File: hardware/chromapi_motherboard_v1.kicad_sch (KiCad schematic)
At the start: 9 parts

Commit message: Updating BOM
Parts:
- H1: now left out of the parts list
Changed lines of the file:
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@@
 		(body_style 1)
 		(exclude_from_sim no)
-		(in_bom yes)
+		(in_bom no)
 		(on_board yes)
 		(in_pos_files yes)

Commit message: Adding MPN to parts
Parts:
- TP1: now left out of the parts list
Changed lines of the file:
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@@
+			)
+		)
+		(property "v" ""
+			(at 156.21 182.88 90)
+			(hide yes)
+			(show_name no)
+			(do_not_autoplace no)
+			(effects
+				(font
+					(size 1.27 1.27)
+				)
 			)
 		)
@@
 			)
 		)
+		(property "v" ""
+			(at 125.73 181.61 0)
+			(hide yes)
+			(show_name no)
+			(do_not_autoplace no)
+			(effects
+				(font
+					(size 1.27 1.27)
+				)
+			)
+		)
 		(instances
 			(project "chromapi_motherboard_v1"
@@
 			)
 		)
+		(property "v" ""
+			(at 149.86 182.88 90)
+			(hide yes)
+			(show_name no)
+			(do_not_autoplace no)
+			(effects
+				(font
+					(size 1.27 1.27)
+				)
+			)
+		)
 		(pin "1"
 		)
@@
 			)
 		)
+		(property "v" ""
+			(at 120.65 189.23 0)
+			(hide yes)
+			(show_name no)
+			(do_not_autoplace no)
+			(effects
+				(font
+					(size 1.27 1.27)
+				)
+			)
+		)
 		(instances
 			(project "chromapi_motherboard_v1"
@@
 			)
 		)
+		(property "v" ""
+			(at 115.57 181.61 0)
+			(hide yes)
+			(show_name no)
+			(do_not_autoplace no)
+			(effects
+				(font
+					(size 1.27 1.27)
+				)
+			)
+		)
 		(instances
 			(project "chromapi_motherboard_v1"
@@
 			)
 		)
+		(property "v" ""
+			(at 143.51 182.88 90)
+			(hide yes)
+			(show_name no)
+			(do_not_autoplace no)
+			(effects
+				(font
+					(size 1.27 1.27)
+				)
+			)
+		)
 		(pin "1"
 		)
@@
 			)
 		)
+		(property "v" ""
+			(at 134.62 168.91 0)
+			(hide yes)
+			(show_name no)
+			(do_not_autoplace no)
+			(effects
+				(font
+					(size 1.27 1.27)
+				)
+			)
+		)
 		(instances
 			(project "chromapi_motherboard_v1"
@@
 		(body_style 1)
 		(exclude_from_sim no)
-		(in_bom yes)
+		(in_bom no)
 		(on_board yes)
 		(in_pos_files yes)
@@
 		)
 		(property "MP" ""
+			(at 140.97 187.96 90)
+			(hide yes)
+			(show_name no)
+			(do_not_autoplace no)
+			(effects
+				(font
+					(size 1.27 1.27)
+				)
+			)
+		)
+		(property "v" ""
 			(at 140.97 187.96 90)
 			(hide yes)
@@
 			(at 162.56 182.88 90)
 			(hide yes)
+			(show_name no)
+			(do_not_autoplace no)
+			(effects
+				(font
+					(size 1.27 1.27)
+				)
+			)
+		)
+		(property "v" ""
+			(at 162.56 182.88 90)
+			(hide yes)

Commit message: Updating schematic
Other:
- note added: "15/04/2026"
- note removed: "JJ/03/2026"

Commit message: note on audio issue
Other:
- note added: "B1"
- note added: "XX/XX/2026"
- note added: "[fixed] correcting the polarity of the connectors for the servomotors"
- note added: "[todo] change the NRST label located on GPIO16 (RPI) to an available position"
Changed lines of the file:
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@@
 		(comment 1 "Ousmane THIONGANE")
+	)
+	(text "[todo] change the NRST label located on GPIO16 (RPI) to an available position"
+		(exclude_from_sim no)
+		(at 182.118 44.704 0)
+		(effects
+			(font
+				(size 1.524 1.524)
+			)
+			(justify left bottom)
+		)
 	)
 	(text "Check"
@@
 		)
 	)
-	(text "Initial drawing"
+	(text "[fixed] correcting the polarity of the connectors for the servomotors"
 		(exclude_from_sim no)
-		(at 181.61 35.56 0)
+		(at 181.864 41.148 0)
+		(effects
+			(font
+				(size 1.524 1.524)
+			)
+			(justify left bottom)
+		)
+	)
+	(text "B1"
+		(exclude_from_sim no)
+		(at 107.696 41.91 0)
 		(effects
 			(font
 				(size 2.0066 2.0066)
+			)
+			(justify left bottom)
+		)
+	)
+	(text "OT"
+		(exclude_from_sim no)
+		(at 152.4 41.91 0)
+		(effects
+			(font
+				(size 2.0066 2.0066)
+			)
+			(justify left bottom)
+		)
+	)
+	(text "Initial drawing"
+		(exclude_from_sim no)
+		(at 181.864 34.798 0)
+		(effects
+			(font
+				(size 1.524 1.524)
 			)
 			(justify left bottom)
@@
 		(effects
 			(font
+				(size 2.0066 2.0066)
+			)
+			(justify left bottom)
+		)
+	)
+	(text "XX/XX/2026"
+		(exclude_from_sim no)
+		(at 128.27 41.656 0)
+		(effects
+			(font

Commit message: adding todo
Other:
- note added: "[todo] check SS34 footprint"
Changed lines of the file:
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@@
+		)
+	)
+	(text "[todo] check SS34 footprint"
+		(exclude_from_sim no)
+		(at 182.118 48.26 0)
+		(effects
+			(font
+				(size 1.524 1.524)
+			)
+			(justify left bottom)
 		)
 	)

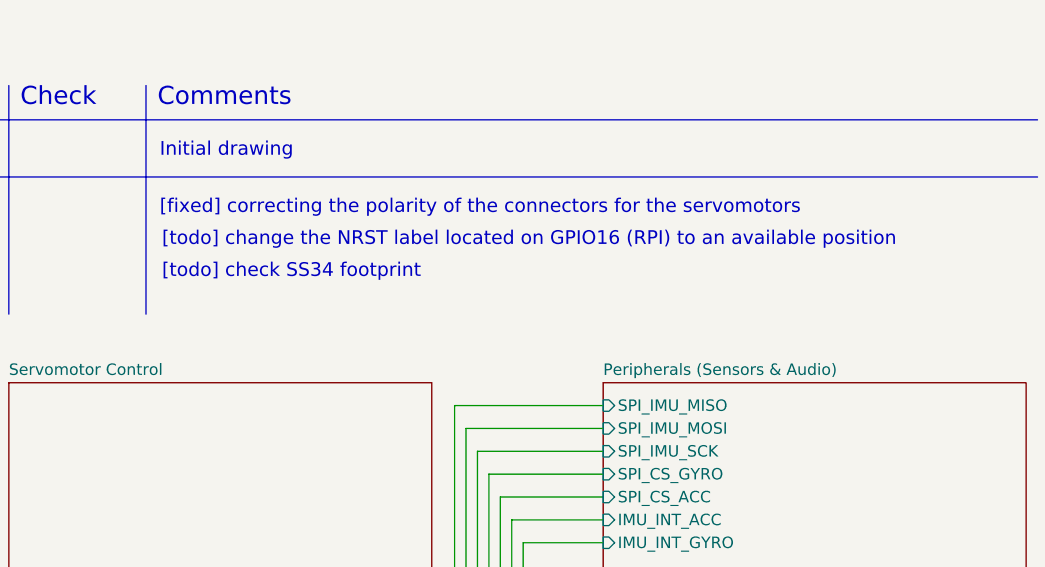
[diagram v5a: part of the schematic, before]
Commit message: Add todo for speaker connector
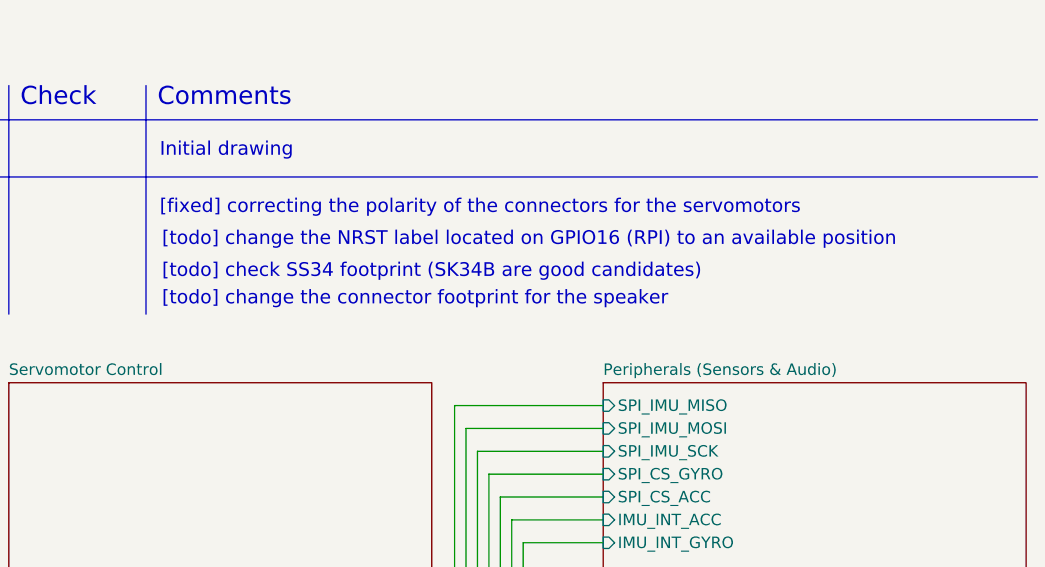
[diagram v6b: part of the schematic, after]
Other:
- note added: "[todo] change the connector footprint for the speaker"
- note added: "[todo] check SS34 footprint (SK34B are good candidates)"
- note removed: "[todo] check SS34 footprint"
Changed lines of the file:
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@@
 		(comment 1 "Ousmane THIONGANE")
+	)
+	(text "[todo] change the connector footprint for the speaker"
+		(exclude_from_sim no)
+		(at 182.118 51.308 0)
+		(effects
+			(font
+				(size 1.524 1.524)
+			)
+			(justify left bottom)
+		)
 	)
 	(text "[todo] change the NRST label located on GPIO16 (RPI) to an available position"
@@
 		)
 	)
-	(text "[todo] check SS34 footprint"
+	(text "[todo] check SS34 footprint (SK34B are good candidates)"
 		(exclude_from_sim no)
 		(at 182.118 48.26 0)

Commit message: update todo list
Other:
- note added: "[todo] check SS34 footprint (SK34B is a good candidate)"
- note added: "[todo] find an alternative to SWD for flashing the STM32"
- note removed: "[todo] check SS34 footprint (SK34B are good candidates)"
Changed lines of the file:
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@@
 	(text "[todo] change the connector footprint for the speaker"
 		(exclude_from_sim no)
-		(at 182.118 51.308 0)
+		(at 182.118 47.498 0)
 		(effects
 			(font
-				(size 1.524 1.524)
+				(size 1.27 1.27)
 			)
 			(justify left bottom)
@@
 	(text "[todo] change the NRST label located on GPIO16 (RPI) to an available position"
 		(exclude_from_sim no)
-		(at 182.118 44.704 0)
+		(at 182.118 42.418 0)
 		(effects
 			(font
-				(size 1.524 1.524)
+				(size 1.27 1.27)
 			)
 			(justify left bottom)
 		)
 	)
-	(text "[todo] check SS34 footprint (SK34B are good candidates)"
+	(text "[todo] check SS34 footprint (SK34B is a good candidate)"
 		(exclude_from_sim no)
-		(at 182.118 48.26 0)
+		(at 182.118 44.958 0)
 		(effects
 			(font
-				(size 1.524 1.524)
+				(size 1.27 1.27)
 			)
 			(justify left bottom)
@@
 	(text "[fixed] correcting the polarity of the connectors for the servomotors"
 		(exclude_from_sim no)
-		(at 181.864 41.148 0)
+		(at 181.864 39.878 0)
 		(effects
 			(font
-				(size 1.524 1.524)
+				(size 1.27 1.27)
 			)
 			(justify left bottom)
@@
 		(exclude_from_sim no)
 		(at 107.696 41.91 0)
+		(effects
+			(font
+				(size 2.0066 2.0066)
+			)
+			(justify left bottom)
+		)
+	)
+	(text "OT"
+		(exclude_from_sim no)
+		(at 166.878 35.56 0)
 		(effects
 			(font
@@
 			)
 			(justify left bottom)
+		)
+	)
+	(text "[todo] find an alternative to SWD for flashing the STM32"
+		(exclude_from_sim no)
+		(at 182.118 50.038 0)
+		(effects
+			(font
+				(size 1.27 1.27)
+			)
+			(justify left bottom)

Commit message: add todos
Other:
- note added: "[todo] move the USB connector to one of the sides of the PCB"
- note added: "[todo] provide a hole for the CSI connector"
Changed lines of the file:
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@@
+		)
+	)
+	(text "[todo] provide a hole for the CSI connector "
+		(exclude_from_sim no)
+		(at 182.118 55.118 0)
+		(effects
+			(font
+				(size 1.27 1.27)
+			)
+			(justify left bottom)
 		)
 	)
@@
 			)
 			(justify left bottom)
+		)
+	)
+	(text "[todo] move the USB connector to one of the sides of the PCB"
+		(exclude_from_sim no)
+		(at 182.118 52.578 0)
+		(effects
+			(font
+				(size 1.27 1.27)
+			)
+			(justify left bottom)
